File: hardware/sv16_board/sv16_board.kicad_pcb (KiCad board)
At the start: 4 copper layers, 100 x 100 mm, 141 parts, among them J1 JTAG, J10 CONSOLE, J2 JTAG-1.27, J3 EXP-A, J4 EXP-B, J5 EXP-C, J6 MOTOR, J7 SPARE (not fitted), J8 USB-C, J9 7-12 V, Q1 2N7002, Q2 BC817, Q4 BC807, SW1 RESET, SW2 RECONFIG, U1 LFE5U-12F-6TG144C, U2 W25Q64JVSSIQ, U3 W25Q64JVSSIQ, U4 CH340G, U5 AP62300TWU-7, U6 MP1584EN, U7 LP5907MFX-2.5, U8 USBLC6-2SC6, Y1 25 MHz ACTIVE XO (4-pin), Y2 12 MHz (CH340G clock)

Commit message: The click-by-click KiCad tutorial, and two footprint names that did not exist
KICAD_TUTORIAL.md / .pdf (root) is the exact how-to for finishing this board, written against this
board's numbers rather than generic advice:

* open the project (and why not to open the bare board), the 141-footprint / 133-net sanity checks
* the one mandatory step - Tools > Update Footprints from Library - and what it preserves
* the floorplan rules that matter here: U1 pin 133 clk, the configuration flash, the USB corner,
  and keeping C38 and the feedback tap where the switcher needs them
* the design rules as the project carries them (Default 0.25 / Power 0.8 / Switching 0.8 with
  0.5 mm clearance / USB 0.2 diff pair / JTAG), plus the extra 0.45-0.2 mm via for the QFP fan-out
* filling the two GND zones, then splitting In2.Cu into the 3V3 / 1V1 / 2V5 pours
* the routing order with widths: power, then the switcher loops, then the 0.5 mm-pitch fan-out,
  then USB as a 0.2/0.2 mm pair with no vias, then clocks, then everything else
* DRC error by error, the 3D check, the exact gerber and drill settings (4.6 mm, PTH+NPTH in one
  file, no Protel extensions), ordering, assembly order and the first power-up voltages
  (3.28 V / 1.10 V / 2.5 V at TP1/TP3/TP2)
* shortcut card, the five ways this goes wrong, and what is still to buy

Also fixed two footprint library IDs the file referenced but the official KiCad libraries do not
contain, which would have broken Update Footprints from Library: the barrel jack is
BarrelJack_CUI_PJ-102AH_Horizontal, and the CD54-class inductor is L_Sunlord_MWSA0518_5.4x5.2mm.
All 36 footprint IDs in the board were then checked against the KiCad footprint repository: none
missing. make tutorial-pdf regenerates the PDF; README and hardware/README point at it.

Co-authored-by: arena-agent <297053741+arena-agent@users.noreply.github.com>
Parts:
- J9: footprint Connector_BarrelJack:BarrelJack_CUI_PJ-102A_Horizontal -> Connector_BarrelJack:BarrelJack_CUI_PJ-102AH_Horizontal
- L1, L2: footprint Inductor_SMD:L_Sunlord_SWPA6045S -> Inductor_SMD:L_Sunlord_MWSA0518_5.4x5.2mm
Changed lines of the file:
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@@
     (pad "2" smd rect (at 2.000 0.000) (size 1.600 2.000) (layers "F.Cu" "F.Paste" "F.Mask") (net 1 "GND"))
   )
-  (footprint "Inductor_SMD:L_Sunlord_SWPA6045S" (layer "F.Cu") (at 42.00 8.00 0) (attr smd)
+  (footprint "Inductor_SMD:L_Sunlord_MWSA0518_5.4x5.2mm" (layer "F.Cu") (at 42.00 8.00 0) (attr smd)
     (fp_text reference "L1" (at 0 -1.6) (layer "F.SilkS") (effects (font (size 0.8 0.8) (thickness 0.15))))
     (fp_text value "10 uH" (at 0 1.6) (layer "F.Fab") (effects (font (size 0.8 0.8) (thickness 0.15))))
@@
     (pad "2" smd rect (at 2.500 0.000) (size 3.400 2.600) (layers "F.Cu" "F.Paste" "F.Mask") (net 4 "3V3"))
   )
-  (footprint "Inductor_SMD:L_Sunlord_SWPA6045S" (layer "F.Cu") (at 32.00 19.00 0) (attr smd)
+  (footprint "Inductor_SMD:L_Sunlord_MWSA0518_5.4x5.2mm" (layer "F.Cu") (at 32.00 19.00 0) (attr smd)
     (fp_text reference "L2" (at 0 -1.6) (layer "F.SilkS") (effects (font (size 0.8 0.8) (thickness 0.15))))
     (fp_text value "10 uH" (at 0 1.6) (layer "F.Fab") (effects (font (size 0.8 0.8) (thickness 0.15))))
@@
     (pad "S4" smd rect (at 3.000 -3.600) (size 1.200 2.400) (layers "F.Cu" "F.Paste" "F.Mask") (net 1 "GND"))
   )
-  (footprint "Connector_BarrelJack:BarrelJack_CUI_PJ-102A_Horizontal" (layer "F.Cu") (at 10.00 10.00 0) (attr through_hole)
+  (footprint "Connector_BarrelJack:BarrelJack_CUI_PJ-102AH_Horizontal" (layer "F.Cu") (at 10.00 10.00 0) (attr through_hole)
     (fp_text reference "J9" (at 0 -1.6) (layer "F.SilkS") (effects (font (size 0.8 0.8) (thickness 0.15))))
     (fp_text value "7-12 V" (at 0 1.6) (layer "F.Fab") (effects (font (size 0.8 0.8) (thickness 0.15))))

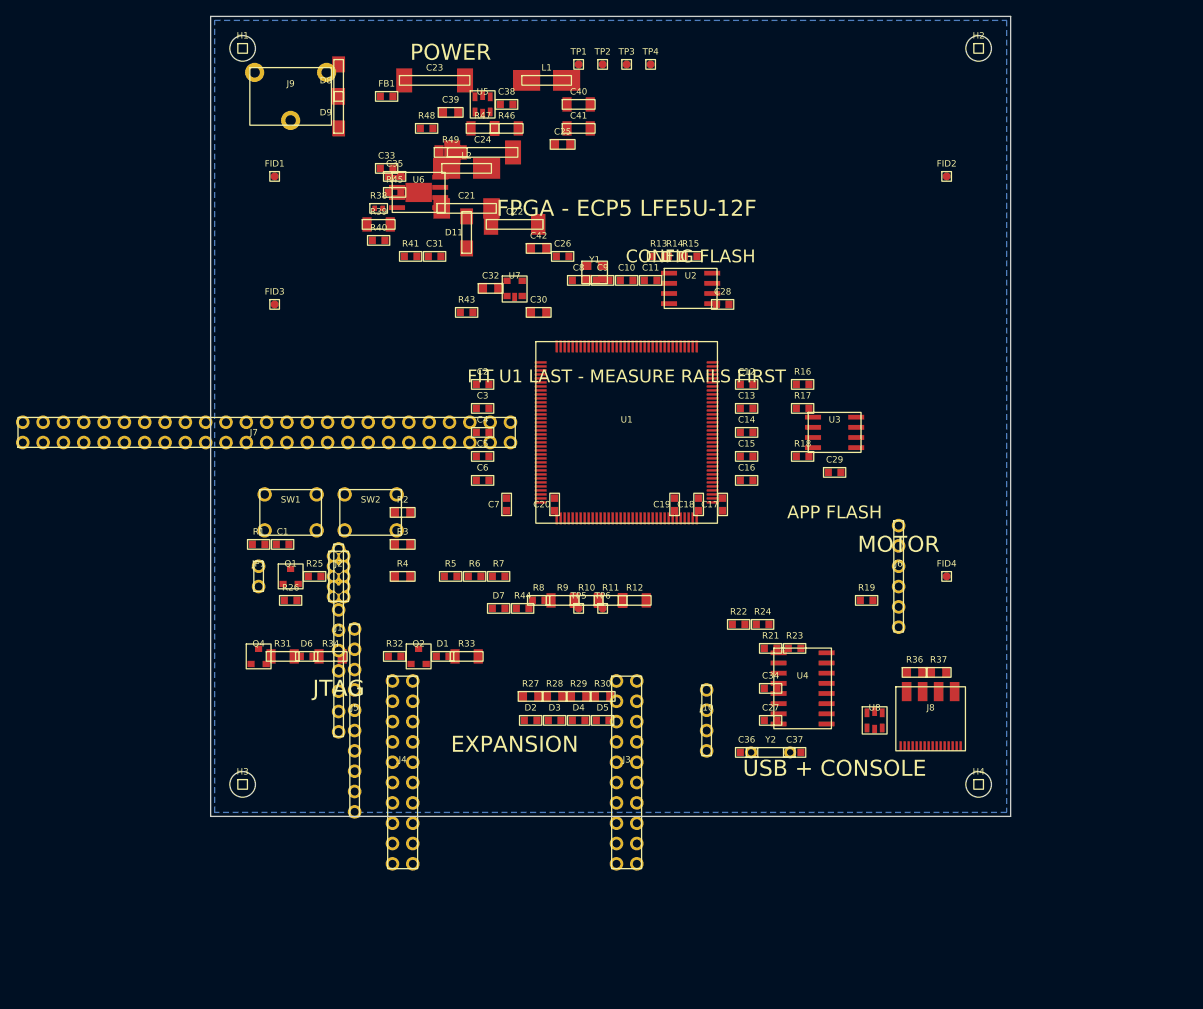
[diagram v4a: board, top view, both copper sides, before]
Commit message: WIP: 0.25 mm U1 land pattern, Power clearance 0.20, maze router, spliced-routing hook
Placement is legal (141 footprints, 0 violations). sv16_route.py does the
4-layer routing in stages: U1 fan-out, plane-net escapes, power spines on
In2.Cu, then signals. sv16_board_kicad.py now splices routing.kicad_pcb.txt
in when it exists so the generated board carries the copper.

Co-authored-by: arena-agent <297053741+arena-agent@users.noreply.github.com>
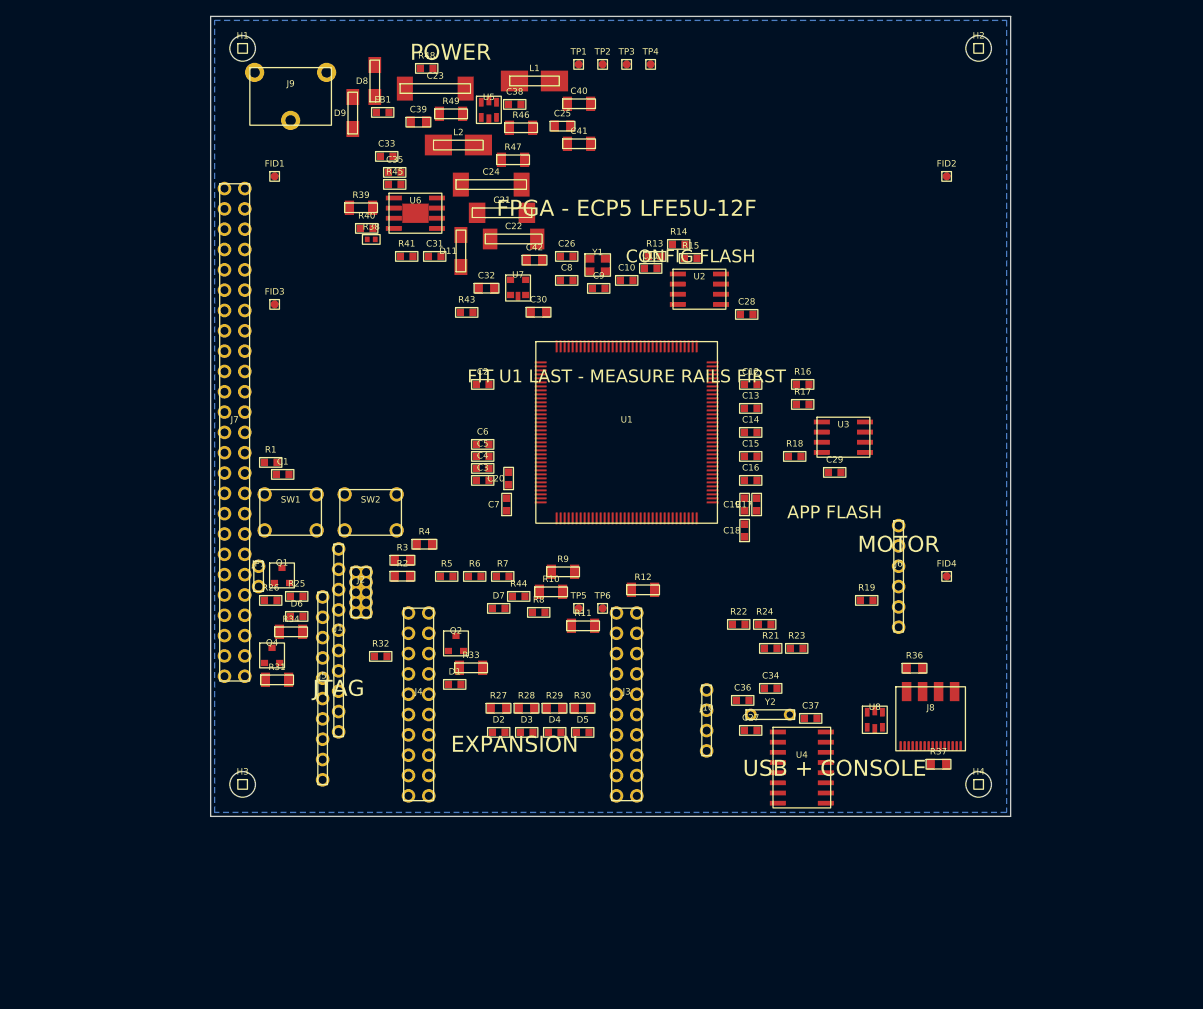
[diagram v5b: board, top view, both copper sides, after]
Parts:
- moved R37 11.5 mm to (91.0, 93.5)
- moved R1 10.4 mm to (7.51, 55.8)
- moved U4 9.90 mm to (73.9, 93.9)
- moved C3 9.00 mm to (34.0, 58.0)
- moved C1 8.75 mm to (9.01, 57.2)
- moved C19 8.75 mm to (66.8, 61.0)
- moved J4 8.73 mm to (26.0, 86.0)
- moved J3 8.50 mm to (52.0, 86.0)
- moved R2 7.98 mm to (24.0, 70.0)
- moved R48 7.50 mm to (27.0, 6.50)
- moved C18 6.61 mm to (66.8, 64.3)
- moved C20 6.60 mm to (37.2, 57.8)
- moved C36 6.52 mm to (66.5, 85.5)
- moved R34 5.82 mm to (10.1, 76.9)
- moved J5 5.66 mm to (14.0, 84.0)
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
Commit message: Board with the power copper routed: openable in KiCad now
Co-authored-by: arena-agent <297053741+arena-agent@users.noreply.github.com>
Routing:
- net 1V1: track 0.00 -> 341.1 mm, vias 0 -> 21
- net 2V5: track 0.00 -> 245.0 mm, vias 0 -> 15
- net VM_IN: track 0.00 -> 203.9 mm, vias 0 -> 10
- net USB_VBUS: track 0.00 -> 139.4 mm, vias 0 -> 6
- net GND: track 0.00 -> 62.6 mm, vias 0 -> 87
- net 3V3: track 0.00 -> 42.7 mm, vias 0 -> 57
- net VM_IN_RAW: track 0.00 -> 15.7 mm, vias 0 -> 3
- net uart_tx: track 0.00 -> 2.00 mm, vias 0 -> 1
- net spi0_sck: track 0.00 -> 2.00 mm, vias 0 -> 1
- net spi0_mosi: track 0.00 -> 2.00 mm, vias 0 -> 1
- net pwm_out: track 0.00 -> 2.00 mm, vias 0 -> 1
- net motor_dir2: track 0.00 -> 2.00 mm, vias 0 -> 1
- net led[3]: track 0.00 -> 2.00 mm, vias 0 -> 1
- net led[1]: track 0.00 -> 2.00 mm, vias 0 -> 1
- net flash_sck: track 0.00 -> 2.00 mm, vias 0 -> 1
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- removed copper zone on B.Cu, net GND
- removed copper zone on In1.Cu, net GND

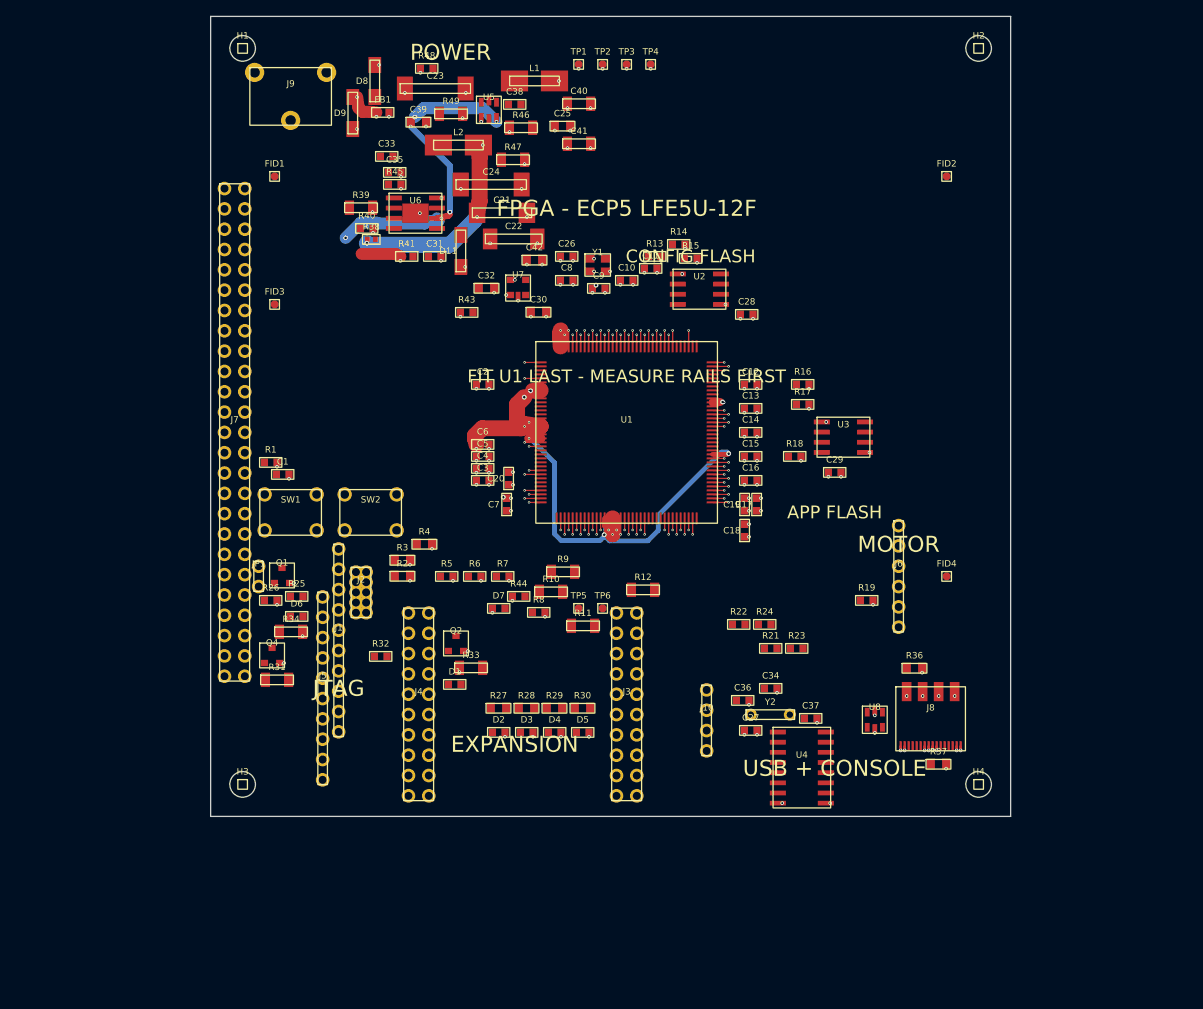
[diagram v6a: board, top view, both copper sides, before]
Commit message: Grow the board to 122 x 122 mm to give the router room
The 100 mm board was too tight: 40 nets ended with pins walled in by tracks
routed before them, and the result looked like a mess rather than a board.
The placement is scaled out by 22% about the centre, so every gap between
parts grows by that much, and the board outline, mounting holes, fiducials
and silkscreen labels move with it.

The fan-out ring and body outline were hard-coded around U1's old position at
(52, 52). They are derived from where U1 actually sits now, so the chip can be
moved without the router silently aiming at empty board.

Co-authored-by: arena-agent <297053741+arena-agent@users.noreply.github.com>
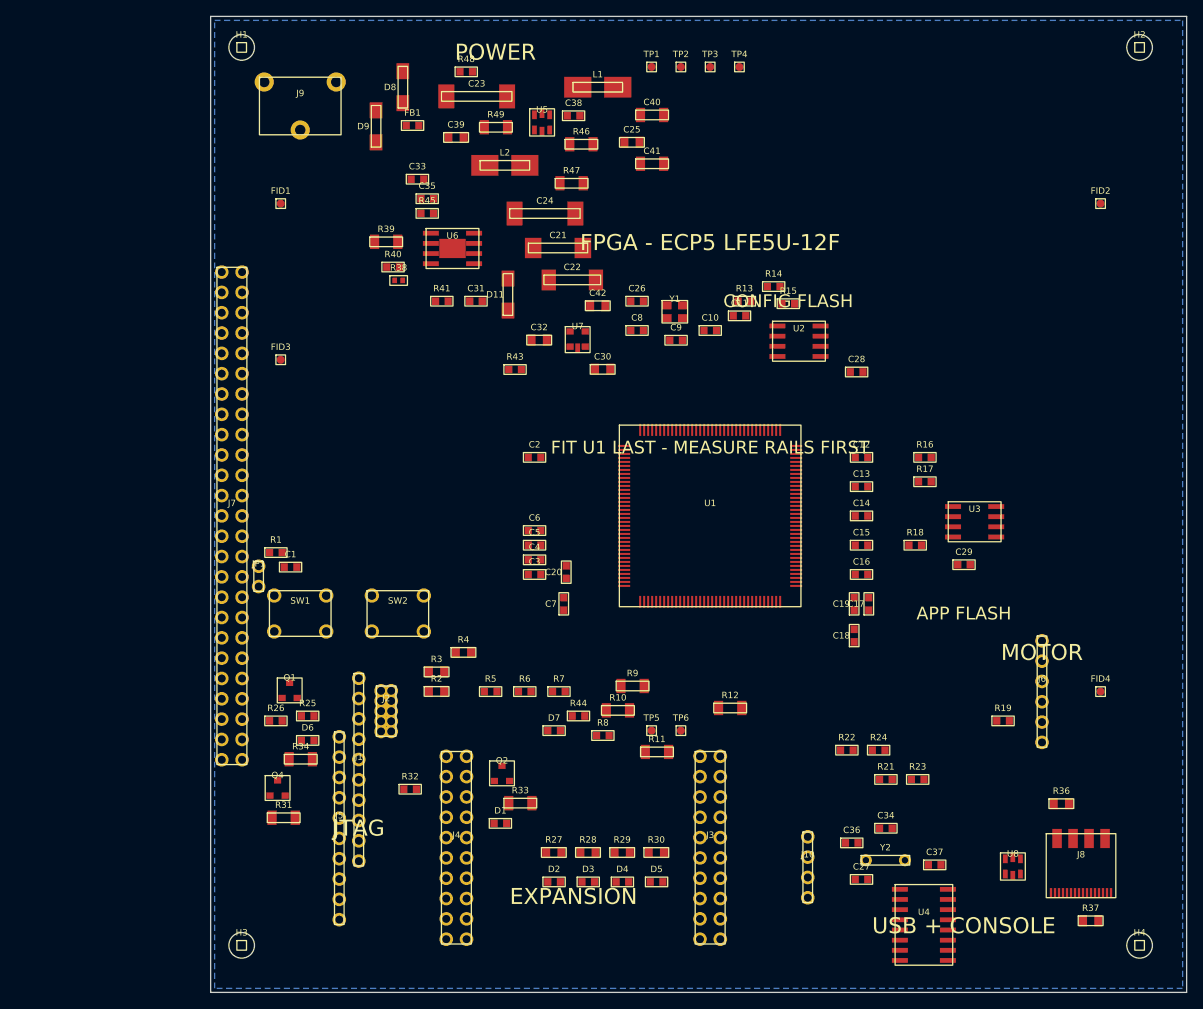
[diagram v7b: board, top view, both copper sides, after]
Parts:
- moved H4 28.5 mm to (116.1, 116.1)
- moved R37 27.3 mm to (110.0, 113.0)
- moved J8 26.3 mm to (108.8, 106.4)
- moved U8 25.2 mm to (100.3, 106.3)
- moved R36 25.0 mm to (106.3, 98.4)
- moved U4 24.9 mm to (89.2, 113.6)
- moved FID4 24.0 mm to (111.2, 84.4)
- moved C37 24.0 mm to (90.5, 106.1)
- moved C27 23.2 mm to (81.4, 107.9)
- moved Y2 23.2 mm to (84.3, 105.5)
- moved J6 23.0 mm to (103.9, 84.4)
- moved R19 22.7 mm to (99.0, 88.1)
- moved C34 22.6 mm to (84.4, 101.5)
- moved C36 22.4 mm to (80.1, 103.3)
- moved R23 22.3 mm to (88.4, 95.4)
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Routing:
- net 1V1: track 341.1 -> 0.00 mm, vias 21 -> 0
- net 2V5: track 245.0 -> 0.00 mm, vias 15 -> 0
- net VM_IN: track 203.9 -> 0.00 mm, vias 10 -> 0
- net USB_VBUS: track 139.4 -> 0.00 mm, vias 6 -> 0
- net GND: track 62.6 -> 0.00 mm, vias 87 -> 0
- net 3V3: track 42.7 -> 0.00 mm, vias 57 -> 0
- net VM_IN_RAW: track 15.7 -> 0.00 mm, vias 3 -> 0
- net uart_tx: track 2.00 -> 0.00 mm, vias 1 -> 0
- net spi0_sck: track 2.00 -> 0.00 mm, vias 1 -> 0
- net spi0_mosi: track 2.00 -> 0.00 mm, vias 1 -> 0
- net pwm_out: track 2.00 -> 0.00 mm, vias 1 -> 0
- net motor_dir2: track 2.00 -> 0.00 mm, vias 1 -> 0
- net led[3]: track 2.00 -> 0.00 mm, vias 1 -> 0
- net led[1]: track 2.00 -> 0.00 mm, vias 1 -> 0
- net flash_sck: track 2.00 -> 0.00 mm, vias 1 -> 0
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- added copper zone on B.Cu, net GND
- added copper zone on In1.Cu, net GND
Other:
- board size 100 x 100 mm -> 122 x 122 mm
